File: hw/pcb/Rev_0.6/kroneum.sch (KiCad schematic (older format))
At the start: 25 parts, among them J1 USB_B_Micro, SW1 Boot_Mode_Btn, SW2 Ctrl_One_Btn, SW3 Reset_Btn, SW4 Ctrl_Ten_Btn, U1 STM32F042F4Px, U2 MCP1700-3302E_SOT89

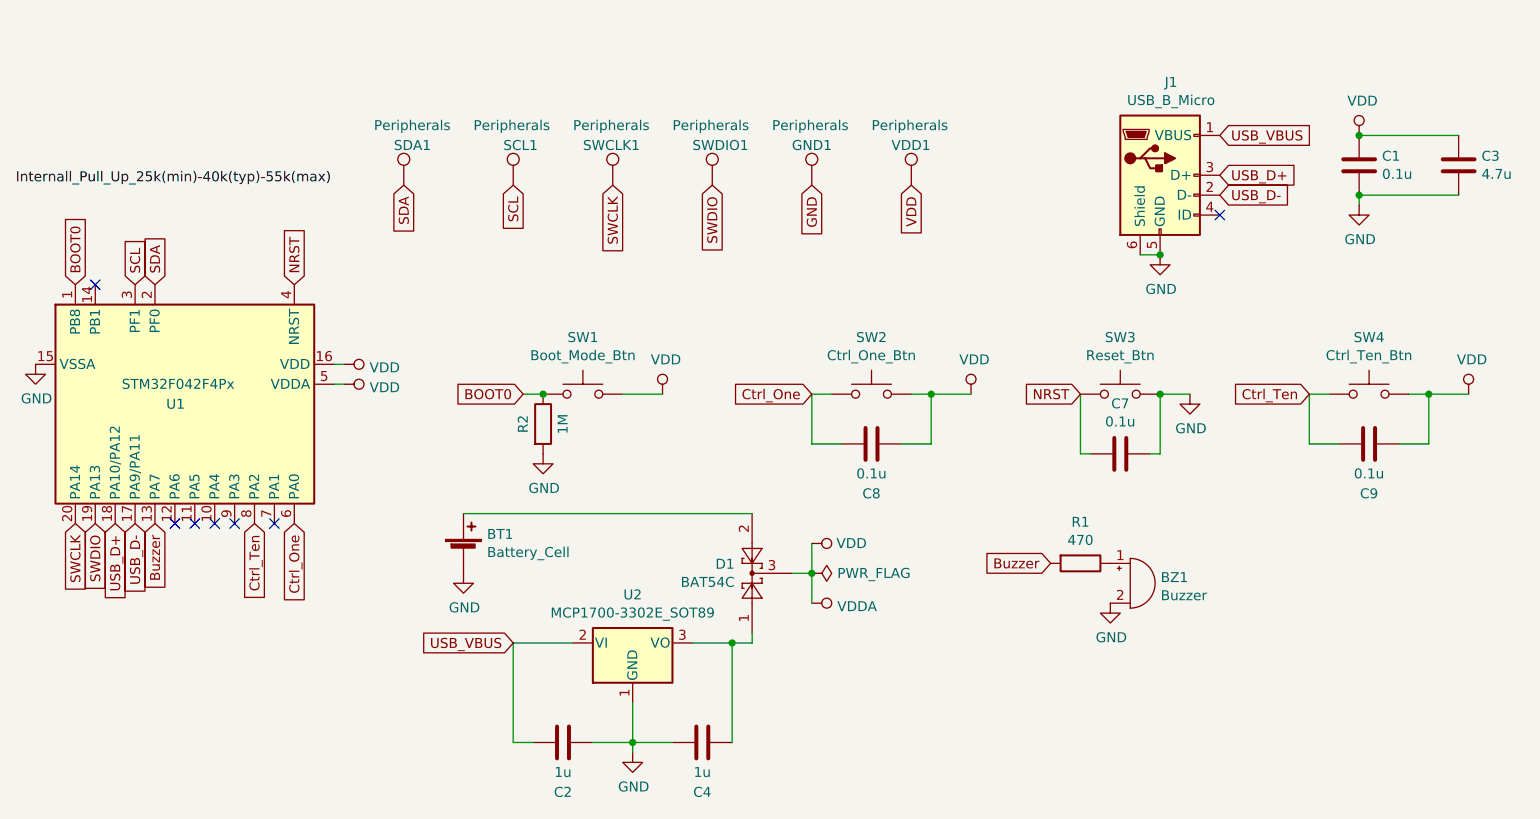
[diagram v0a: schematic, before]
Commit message: [pcb] introduce PCB rev 0.6 (reduced size to 30mmx30mm, exposed all unused pads, moved batter to the back layer)
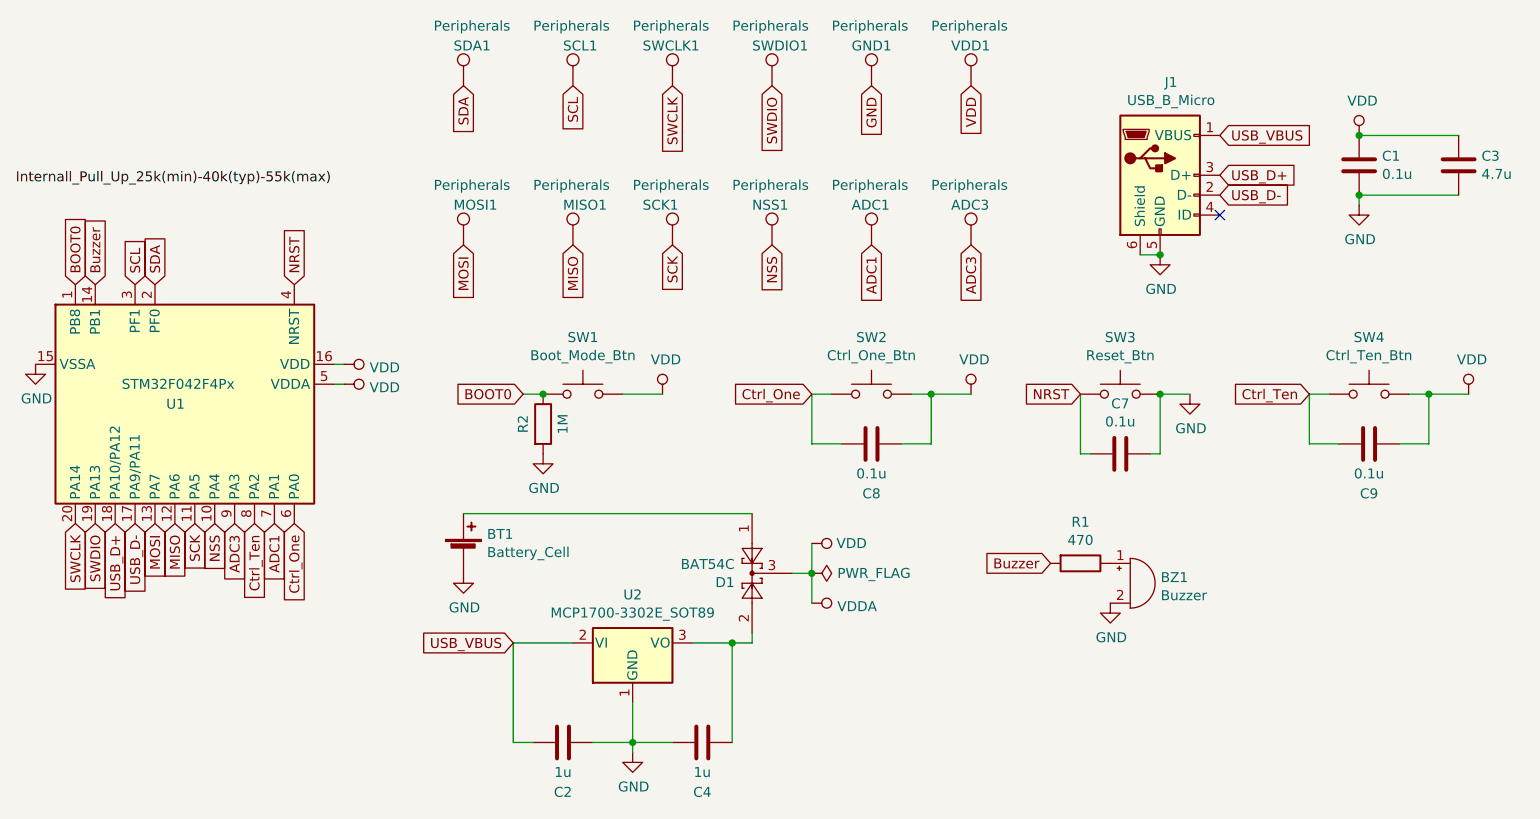
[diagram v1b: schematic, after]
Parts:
- added ADC1, ADC3, MISO1, MOSI1, NSS1, SCK1: Peripherals, TestPoint:TestPoint_THTPad_2.0x2.0mm_Drill1.0mm, symbol Connector:TestPoint
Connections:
- net Buzzer: now also U1.14 (PB1); no longer U1.13 (PA7)
- net NSS: now reaches U1.10 (PA4)
- net NSS: now also NSS1.1
- net SCK: now reaches U1.11 (PA5)
- net SCK: now also SCK1.1
- net MISO: now reaches U1.12 (PA6)
- net MISO: now also MISO1.1
- net ADC1: now reaches U1.7 (PA1)
- net ADC1: now also ADC1.1
- net ADC3: now reaches U1.9 (PA3)
- net ADC3: now also ADC3.1
- net at BT1.1 (+): now also D1.1; no longer D1.2
- net at C4.1, U2.3 (VO): now also D1.2; no longer D1.1
- new net MOSI: MOSI1.1, U1.13 (PA7)
- no-connect marks 7 -> 1
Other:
- moved on the sheet: GND1, SCL1, SDA1, SWCLK1, SWDIO1, VDD1
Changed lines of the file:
@@
 	1    0    0    -1
 $EndComp
-Text GLabel 2400 4050 3    50   Input ~ 0
+Text GLabel 2100 2850 1    50   Input ~ 0
 Buzzer
 Text GLabel 2300 4050 3    50   Input ~ 0
@@
 Text GLabel 2900 4050 3    50   Input ~ 0
 Ctrl_Ten
-NoConn ~ 2500 4050
-NoConn ~ 2600 4050
-NoConn ~ 3000 4050
-NoConn ~ 2800 4050
-NoConn ~ 2700 4050
-NoConn ~ 2100 2850
 $Comp
 L Device:C C8
@@
 F 3 "http://www.diodes.com/_files/datasheets/ds11005.pdf" H 5320 4300 50  0001 C CNN
 	1    5400 4300
-	0    -1   -1   0
+	0    -1   1    0
 $EndComp
 Wire Wire Line
@@
 Text GLabel 2400 2850 1    50   Input ~ 0
 SDA
-Text GLabel 3650 2350 3    50   Input ~ 0
+Text GLabel 3950 1850 3    50   Input ~ 0
 SDA
-Text GLabel 4200 2350 3    50   Input ~ 0
+Text GLabel 4500 1850 3    50   Input ~ 0
 SCL
-Text GLabel 4700 2350 3    50   Input ~ 0
+Text GLabel 5000 1850 3    50   Input ~ 0
 SWCLK
-Text GLabel 5200 2350 3    50   Input ~ 0
+Text GLabel 5500 1850 3    50   Input ~ 0
 SWDIO
 Wire Wire Line
@@
 L Connector:TestPoint SWDIO1
 U 1 1 5C6F9685
-P 5200 2350
-F 0 "SWDIO1" H 5100 2550 50  0000 L CNN
-F 1 "Peripherals" H 5000 2650 50  0000 L CNN
-F 2 "TestPoint:TestPoint_THTPad_2.0x2.0mm_Drill1.0mm" H 5400 2350 50  0001 C CNN
-F 3 "~" H 5400 2350 50  0001 C CNN
-	1    5200 2350
+P 5500 1850
+F 0 "SWDIO1" H 5400 2050 50  0000 L CNN
+F 1 "Peripherals" H 5300 2150 50  0000 L CNN
+F 2 "TestPoint:TestPoint_THTPad_2.0x2.0mm_Drill1.0mm" H 5700 1850 50  0001 C CNN
+F 3 "~" H 5700 1850 50  0001 C CNN
+	1    5500 1850
 	1    0    0    -1
 $EndComp
@@
 L Connector:TestPoint SWCLK1
 U 1 1 5C6F8CE1
-P 4700 2350
-F 0 "SWCLK1" H 4550 2550 50  0000 L CNN
-F 1 "Peripherals" H 4500 2650 50  0000 L CNN
-F 2 "TestPoint:TestPoint_THTPad_2.0x2.0mm_Drill1.0mm" H 4900 2350 50  0001 C CNN
-F 3 "~" H 4900 2350 50  0001 C CNN
-	1    4700 2350
+P 5000 1850
+F 0 "SWCLK1" H 4850 2050 50  0000 L CNN
+F 1 "Peripherals" H 4800 2150 50  0000 L CNN
+F 2 "TestPoint:TestPoint_THTPad_2.0x2.0mm_Drill1.0mm" H 5200 1850 50  0001 C CNN
+F 3 "~" H 5200 1850 50  0001 C CNN
+	1    5000 1850
 	1    0    0    -1
 $EndComp
@@
 L Connector:TestPoint SCL1
 U 1 1 5C6F8355
-P 4200 2350
-F 0 "SCL1" H 4150 2550 50  0000 L CNN
-F 1 "Peripherals" H 4000 2650 50  0000 L CNN
-F 2 "TestPoint:TestPoint_THTPad_2.0x2.0mm_Drill1.0mm" H 4400 2350 50  0001 C CNN
-F 3 "~" H 4400 2350 50  0001 C CNN
-	1    4200 2350
+P 4500 1850
+F 0 "SCL1" H 4450 2050 50  0000 L CNN
+F 1 "Peripherals" H 4300 2150 50  0000 L CNN
+F 2 "TestPoint:TestPoint_THTPad_2.0x2.0mm_Drill1.0mm" H 4700 1850 50  0001 C CNN
+F 3 "~" H 4700 1850 50  0001 C CNN
+	1    4500 1850
 	1    0    0    -1
 $EndComp
@@
 L Connector:TestPoint SDA1
 U 1 1 5C6F2C19
-P 3650 2350
-F 0 "SDA1" H 3600 2550 50  0000 L CNN
-F 1 "Peripherals" H 3500 2650 50  0000 L CNN
-F 2 "TestPoint:TestPoint_THTPad_2.0x2.0mm_Drill1.0mm" H 3850 2350 50  0001 C CNN
-F 3 "~" H 3850 2350 50  0001 C CNN
-	1    3650 2350
-	1    0    0    -1
-$EndComp
-Text GLabel 5700 2350 3    50   Input ~ 0
+P 3950 1850
+F 0 "SDA1" H 3900 2050 50  0000 L CNN
+F 1 "Peripherals" H 3800 2150 50  0000 L CNN
+F 2 "TestPoint:TestPoint_THTPad_2.0x2.0mm_Drill1.0mm" H 4150 1850 50  0001 C CNN
+F 3 "~" H 4150 1850 50  0001 C CNN
+	1    3950 1850
+	1    0    0    -1
+$EndComp
+Text GLabel 6000 1850 3    50   Input ~ 0
 GND
 $Comp
 L Connector:TestPoint GND1
 U 1 1 5D81E1ED
-P 5700 2350
-F 0 "GND1" H 5600 2550 50  0000 L CNN
-F 1 "Peripherals" H 5500 2650 50  0000 L CNN
-F 2 "TestPoint:TestPoint_THTPad_2.0x2.0mm_Drill1.0mm" H 5900 2350 50  0001 C CNN
-F 3 "~" H 5900 2350 50  0001 C CNN
-	1    5700 2350
-	1    0    0    -1
-$EndComp
-Text GLabel 6200 2350 3    50   Input ~ 0
+P 6000 1850
+F 0 "GND1" H 5900 2050 50  0000 L CNN
+F 1 "Peripherals" H 5800 2150 50  0000 L CNN
+F 2 "TestPoint:TestPoint_THTPad_2.0x2.0mm_Drill1.0mm" H 6200 1850 50  0001 C CNN
+F 3 "~" H 6200 1850 50  0001 C CNN
+	1    6000 1850
+	1    0    0    -1
+$EndComp
+Text GLabel 6500 1850 3    50   Input ~ 0
 VDD
 $Comp
 L Connector:TestPoint VDD1
 U 1 1 5D81EFFF
-P 6200 2350
-F 0 "VDD1" H 6100 2550 50  0000 L CNN
-F 1 "Peripherals" H 6000 2650 50  0000 L CNN
-F 2 "TestPoint:TestPoint_THTPad_2.0x2.0mm_Drill1.0mm" H 6400 2350 50  0001 C CNN
-F 3 "~" H 6400 2350 50  0001 C CNN
-	1    6200 2350
-	1    0    0    -1
-$EndComp
+P 6500 1850
+F 0 "VDD1" H 6400 2050 50  0000 L CNN
+F 1 "Peripherals" H 6300 2150 50  0000 L CNN
+F 2 "TestPoint:TestPoint_THTPad_2.0x2.0mm_Drill1.0mm" H 6700 1850 50  0001 C CNN
+F 3 "~" H 6700 1850 50  0001 C CNN
+	1    6500 1850
+	1    0    0    -1
+$EndComp
+Text GLabel 2400 4050 3    50   Input ~ 0
+MOSI
+Text GLabel 2500 4050 3    50   Input ~ 0
+MISO
+Text GLabel 2600 4050 3    50   Input ~ 0
+SCK
+Text GLabel 2700 4050 3    50   Input ~ 0
+NSS
+Text GLabel 2800 4050 3    50   Input ~ 0
+ADC3
+Text GLabel 3000 4050 3    50   Input ~ 0
+ADC1
+Text GLabel 3950 2650 3    50   Input ~ 0
+MOSI
+Text GLabel 4500 2650 3    50   Input ~ 0
+MISO
+Text GLabel 5000 2650 3    50   Input ~ 0
+SCK
+Text GLabel 5500 2650 3    50   Input ~ 0
+NSS
+$Comp
+L Connector:TestPoint NSS1
+U 1 1 5D94D78C
+P 5500 2650
+F 0 "NSS1" H 5400 2850 50  0000 L CNN
+F 1 "Peripherals" H 5300 2950 50  0000 L CNN
+F 2 "TestPoint:TestPoint_THTPad_2.0x2.0mm_Drill1.0mm" H 5700 2650 50  0001 C CNN
+F 3 "~" H 5700 2650 50  0001 C CNN
+	1    5500 2650
+	1    0    0    -1
+$EndComp
+$Comp
+L Connector:TestPoint SCK1
+U 1 1 5D94D792
+P 5000 2650
+F 0 "SCK1" H 4850 2850 50  0000 L CNN
+F 1 "Peripherals" H 4800 2950 50  0000 L CNN
+F 2 "TestPoint:TestPoint_THTPad_2.0x2.0mm_Drill1.0mm" H 5200 2650 50  0001 C CNN
+F 3 "~" H 5200 2650 50  0001 C CNN
+	1    5000 2650
+	1    0    0    -1
+$EndComp
+$Comp
+L Connector:TestPoint MISO1
+U 1 1 5D94D798
+P 4500 2650
+F 0 "MISO1" H 4450 2850 50  0000 L CNN
+F 1 "Peripherals" H 4300 2950 50  0000 L CNN
+F 2 "TestPoint:TestPoint_THTPad_2.0x2.0mm_Drill1.0mm" H 4700 2650 50  0001 C CNN
+F 3 "~" H 4700 2650 50  0001 C CNN
+	1    4500 2650
+	1    0    0    -1
+$EndComp
+$Comp
+L Connector:TestPoint MOSI1
+U 1 1 5D94D79E
+P 3950 2650
+F 0 "MOSI1" H 3900 2850 50  0000 L CNN
+F 1 "Peripherals" H 3800 2950 50  0000 L CNN
+F 2 "TestPoint:TestPoint_THTPad_2.0x2.0mm_Drill1.0mm" H 4150 2650 50  0001 C CNN
+F 3 "~" H 4150 2650 50  0001 C CNN
+	1    3950 2650
+	1    0    0    -1
+$EndComp
+Text GLabel 6000 2650 3    50   Input ~ 0
+ADC1
+$Comp
+L Connector:TestPoint ADC1
+U 1 1 5D94D7A5
+P 6000 2650
+F 0 "ADC1" H 5900 2850 50  0000 L CNN
+F 1 "Peripherals" H 5800 2950 50  0000 L CNN
+F 2 "TestPoint:TestPoint_THTPad_2.0x2.0mm_Drill1.0mm" H 6200 2650 50  0001 C CNN
+F 3 "~" H 6200 2650 50  0001 C CNN
+	1    6000 2650
+	1    0    0    -1
+$EndComp
+Text GLabel 6500 2650 3    50   Input ~ 0
+ADC3
+$Comp
+L Connector:TestPoint ADC3
+U 1 1 5D94D7AC
+P 6500 2650
+F 0 "ADC3" H 6400 2850 50  0000 L CNN
+F 1 "Peripherals" H 6300 2950 50  0000 L CNN
+F 2 "TestPoint:TestPoint_THTPad_2.0x2.0mm_Drill1.0mm" H 6700 2650 50  0001 C CNN
+F 3 "~" H 6700 2650 50  0001 C CNN
+	1    6500 2650
+	1    0    0    -1
+$EndComp
